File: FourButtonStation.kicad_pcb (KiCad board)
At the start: 2 copper layers, 106 x 65 mm, 83 parts, among them J1 AC IN, J10 AC IN, J11 AC IN, J2 External 3V, J3 UART, J4 ADC, J5 Conn_WallSocket, J7 Conn_WallSocket, J8 Conn_WallSocket, J9 Conn_WallSocket, K1 G5LE-1, K2 G5LE-1, K3 G5LE-1, K4 G5LE-1, Q1 MMBT3904, Q3 MMBT3904, SW1 POWER, SW2 RST, SW5 Mode, U1 CH340C, U10 SM4007PL, U11 D882_C9634, U13 AMS1117-3_3, U2 radio-receiver, U3 ESP-07, U4 SM4007PL, U5 D882_C9634, U6 SM4007PL, U7 D882_C9634, U8 SM4007PL, U9 D882_C9634

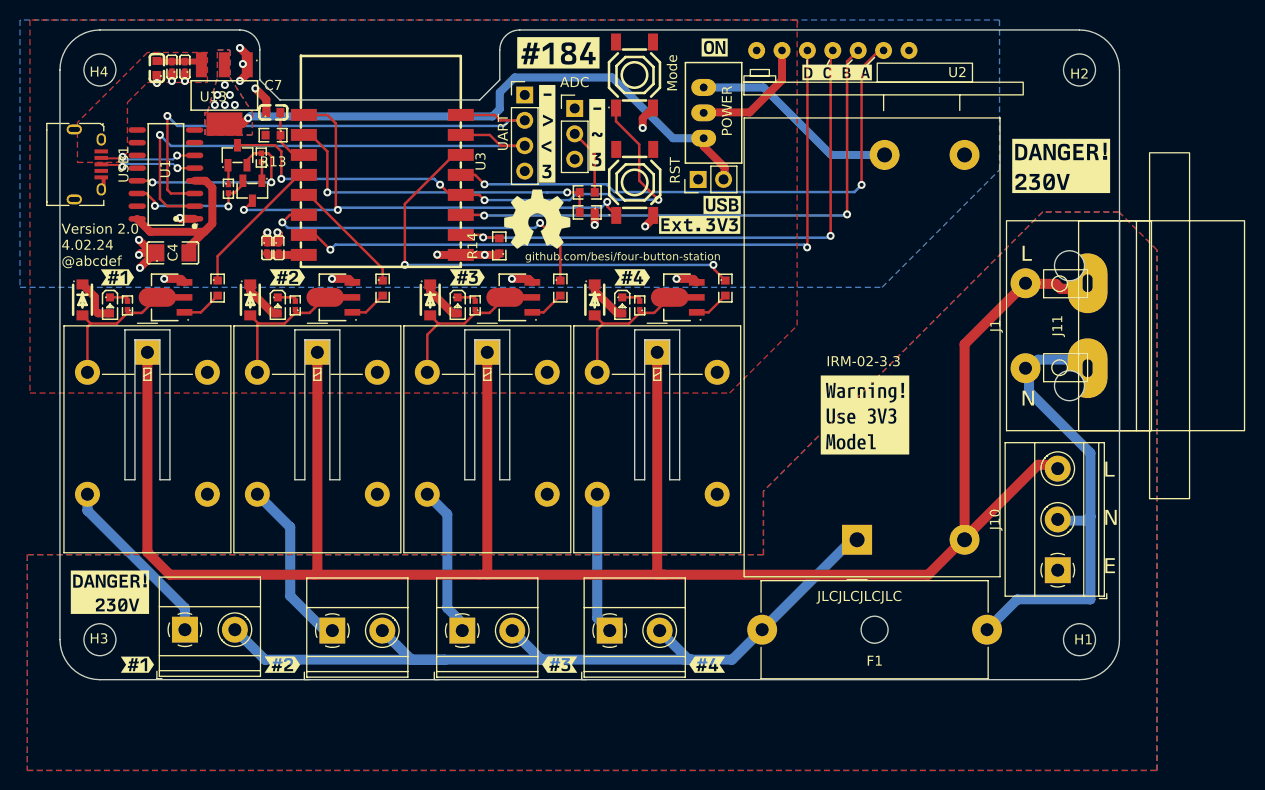
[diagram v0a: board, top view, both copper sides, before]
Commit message: Silk screen and add Earth Vias
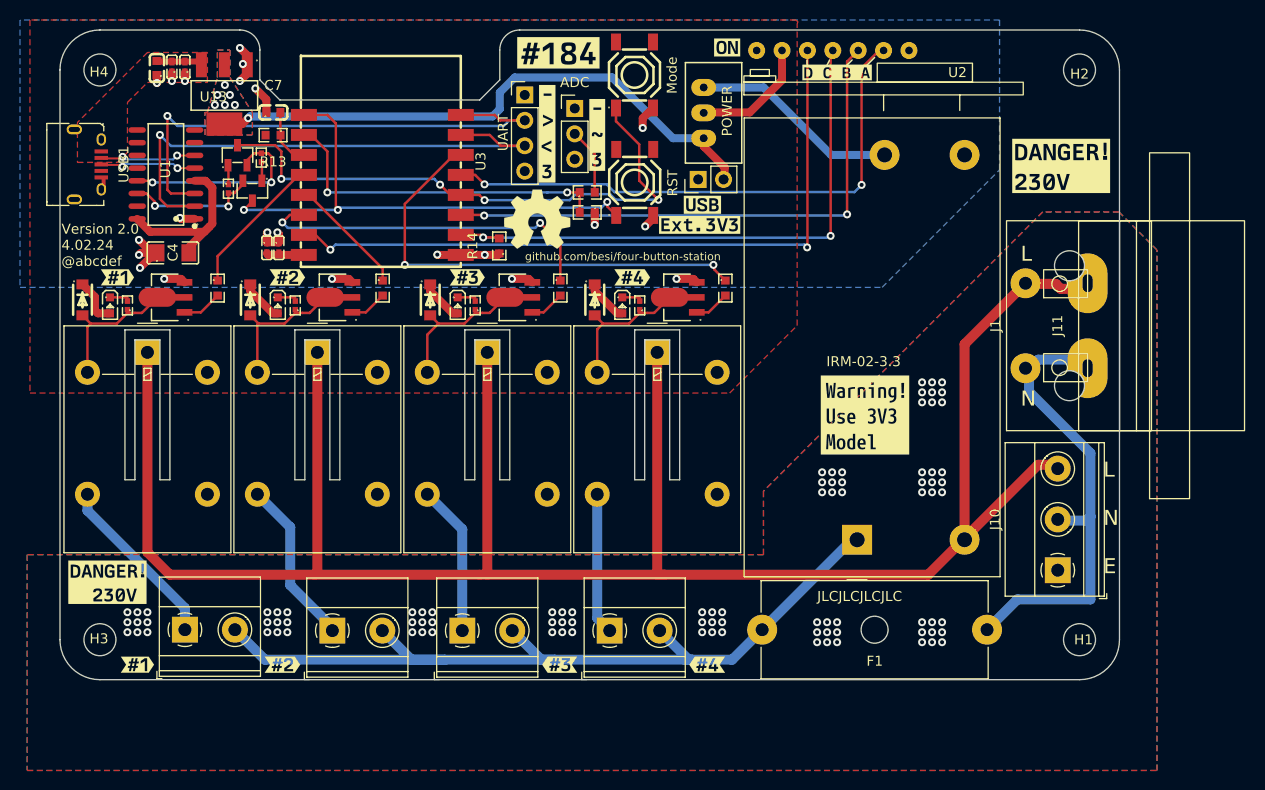
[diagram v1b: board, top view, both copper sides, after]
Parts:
- moved kibuzzard-65EE298C 1.98 mm to (81.5, 107.2)
- moved kibuzzard-65EE261E 1.25 mm to (84.0, 91.5)
- moved kibuzzard-65F05324 1.03 mm to (22.0, 145.0)
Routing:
- net Earth: vias 0 -> 90

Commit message: Prepare for deployment
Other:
- board text added: "Version 2.0 5.02.24 @abcdef"
- board text removed: "Version 2.0 4.02.24 @abcdef"
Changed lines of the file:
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@@
     (effects (font (size 1.5 1.5) (thickness 0.2)) (justify left bottom))
   )
-  (gr_text "Version 2.0\n4.02.24\n@abcdef" (at 17.396907 113.472428) (layer "F.SilkS")
+  (gr_text "Version 2.0\n5.02.24\n@abcdef" (at 17.396907 113.472428) (layer "F.SilkS")
     (effects (font (size 1 1) (thickness 0.15)) (justify left bottom))
   )

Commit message: Prepare for upcoming version 2.1-beta
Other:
- board text added: "v2.1-beta {DATE} @aabbcc"
- board text removed: "Version 2.0 5.02.24 @abcdef"
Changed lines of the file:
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@@
     (property "Sheetfile" "FourButtonStation.kicad_sch")
     (property "Sheetname" "")
+    (property "exclude_from_bom" "")
     (property "ki_description" "Generic screw terminal, single row, 01x03, script generated (kicad-library-utils/schlib/autogen/connector/)")
     (property "ki_keywords" "screw terminal")
-    (attr through_hole)
+    (attr through_hole exclude_from_bom)
     (fp_text reference "J10" (at 5.08 -6.26 90) (layer "F.SilkS")
         (effects (font (size 1 1) (thickness 0.15)))
@@
     (property "Sheetname" "")
     (property "exclude_from_bom" "")
-    (attr through_hole exclude_from_bom)
+    (attr through_hole exclude_from_pos_files exclude_from_bom)
     (fp_text reference "J11" (at 0 -3 90 unlocked) (layer "F.SilkS")
         (effects (font (size 1 1) (thickness 0.15)))
@@
     (property "Sheetname" "")
     (property "exclude_from_bom" "")
-    (attr through_hole exclude_from_bom)
+    (attr through_hole exclude_from_pos_files exclude_from_bom)
     (fp_text reference "J1" (at 0 -3 90 unlocked) (layer "F.SilkS")
         (effects (font (size 1 1) (thickness 0.15)))
@@
     (effects (font (size 1.5 1.5) (thickness 0.2)) (justify left bottom))
   )
-  (gr_text "Version 2.0\n5.02.24\n@abcdef" (at 17.396907 113.472428) (layer "F.SilkS")
+  (gr_text "v2.1-beta\n{DATE}\n@aabbcc" (at 17.5 113.472428) (layer "F.SilkS")
     (effects (font (size 1 1) (thickness 0.15)) (justify left bottom))
   )
